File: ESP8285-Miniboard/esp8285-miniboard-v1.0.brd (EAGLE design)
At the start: 35.9 x 15.5 mm, 40 parts, among them Q1 FA-128

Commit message: Another Rev 1.0
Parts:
- moved C4 0.06 mm to (32.6, 22.0)
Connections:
- net N$IO1: now also PROG.2
- net N$IO2: no longer PROG.2
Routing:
- net N$IO2: track 23.4 -> 6.94 mm, vias 2 -> 0
- net N$IO1: track 20.2 -> 30.9 mm, vias 2 -> 3
- net N$IO3: track 24.6 -> 27.1 mm
- net N$3: track 1.55 -> 0.00 mm

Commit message: Hopefully final V1.0
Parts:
- added CH_PU: (no value), Ma-ESP8285:TESTPIN-HDR1X01
- moved 0 16.3 mm to (7.87, 14.2)
- moved 10 16.3 mm to (7.87, 1.46)
- moved 12 16.3 mm to (18.0, 14.2)
- moved 8 16.3 mm to (18.0, 1.46)
- moved R3 16.3 mm to (8.51, 8.45)
- moved 1 16.3 mm to (25.7, 1.46)
- moved 11 16.3 mm to (10.4, 1.46)
- moved 13 16.3 mm to (15.5, 14.2)
- moved 14 16.3 mm to (20.6, 14.2)
- moved 15 16.3 mm to (13.0, 14.2)
- moved 16 16.3 mm to (23.1, 14.2)
- moved 2 16.3 mm to (10.4, 14.2)
- moved 3 16.3 mm to (23.1, 1.46)
- moved 3V3 16.3 mm to (28.2, 14.2)
- moved 4 16.3 mm to (5.33, 14.2)
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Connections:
- net N$CHIP_PU: now also CH_PU.1
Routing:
- net GND: track 53.4 -> 74.1 mm, vias 9 -> 17
- net N$9: track 13.9 -> 0.00 mm
- net +3V3: track 65.4 -> 73.3 mm
- net N$4: track 7.00 -> 0.00 mm
- net N$7: track 5.84 -> 0.00 mm
- net N$5: track 4.23 -> 0.00 mm
- net N$IO1: track 30.9 -> 34.8 mm
- net N$IO15: track 14.6 -> 18.4 mm
- net N$IO3: track 27.1 -> 29.2 mm
- net N$6: track 1.44 -> 0.00 mm
- net N$CHIP_PU: track 11.4 -> 10.4 mm, vias 2 -> 1
- net N$IO2: track 6.94 -> 7.53 mm
- net N$IO0: track 22.9 -> 23.5 mm
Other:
- board text added: "Pwr"
- board text added: "Rx"
- board text added: "Tx"
- board text removed: "RX"
- board text removed: "TX"

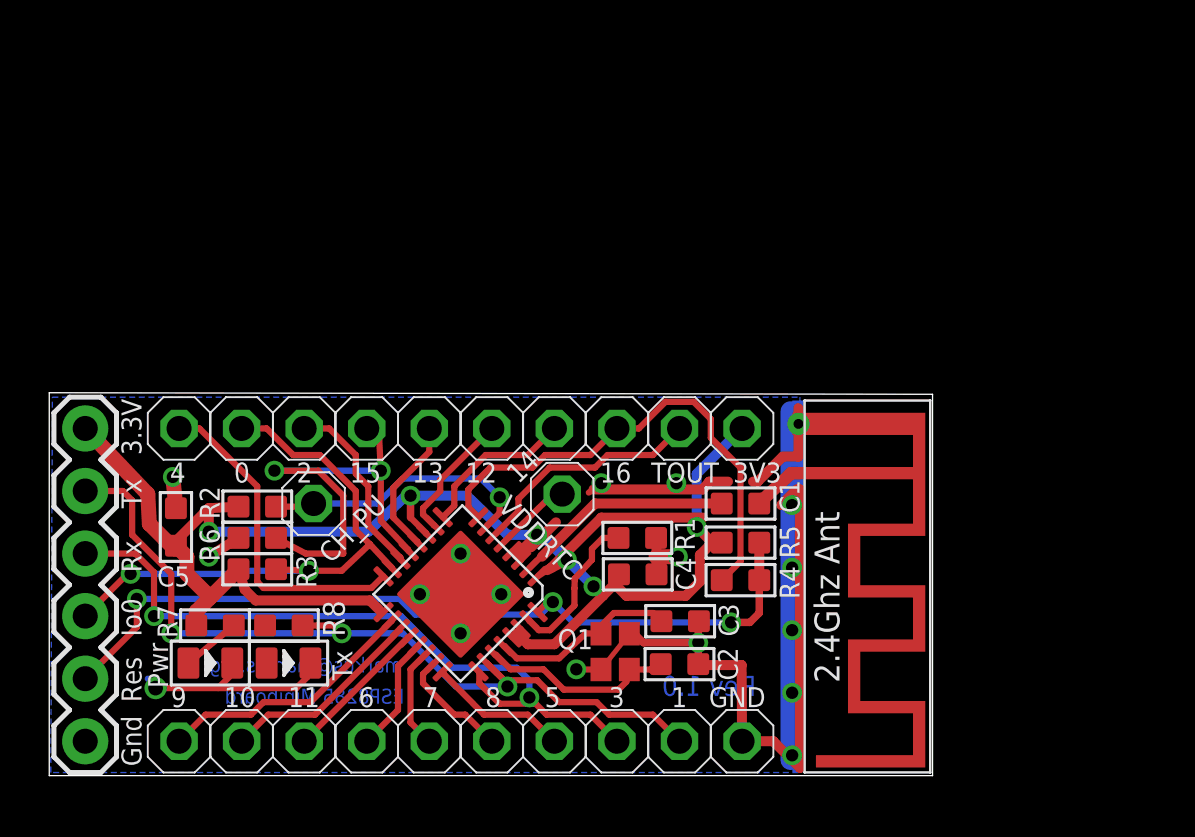
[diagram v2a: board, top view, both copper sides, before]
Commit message: Final v1.0 fixed silkscreen, added testpoint, reduced via size
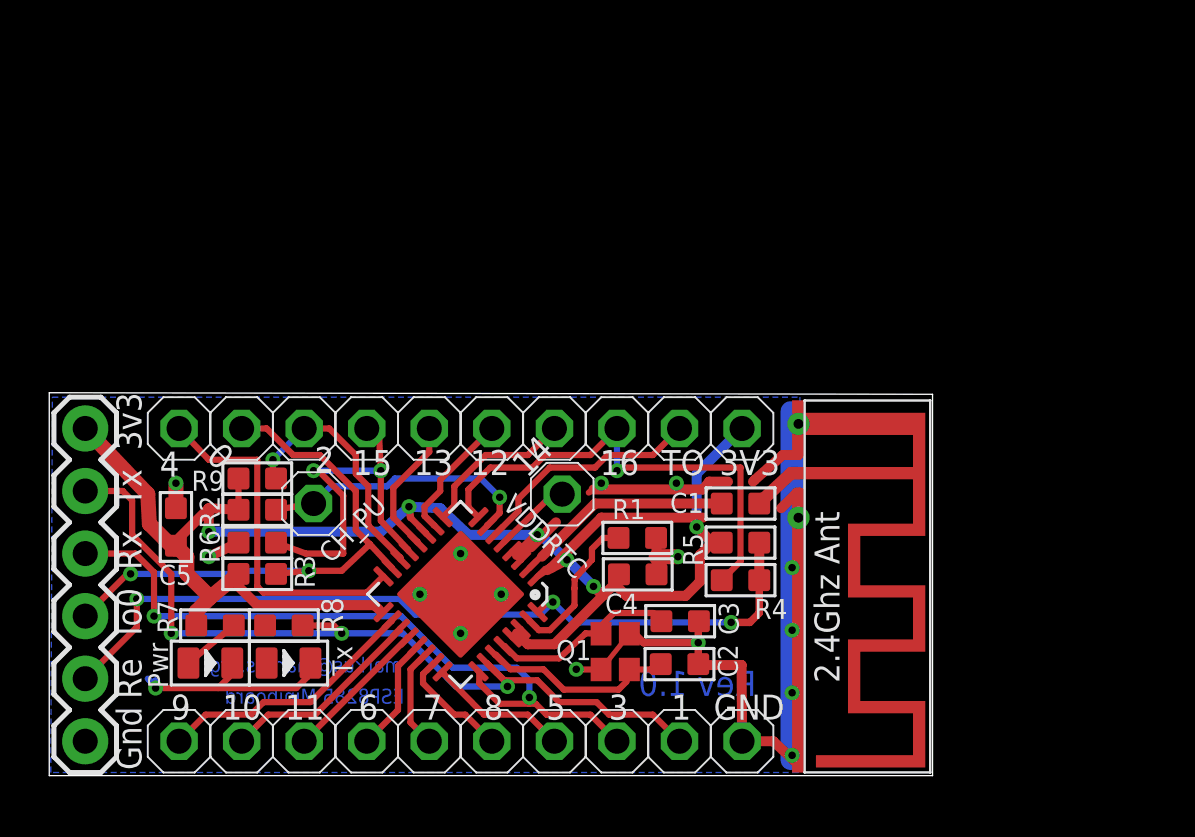
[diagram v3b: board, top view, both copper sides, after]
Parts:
- removed TOUT: (no value), Ma-ESP8285:TESTPIN-HDR1X01
- added R9: 10K, Seeed-OPL-Resistor:R0603
- added TO: (no value), Markus:TESTPIN-HDR1X01
- 0, 1, 10, 11, 12, 13, 14, 15, 16, 2, 3, 3V3, 4, 5, 6, 7, 8, 9, CH_PU, GND, VDDRTC: device Ma-ESP8285:TESTPIN-HDR1X01 -> Markus:TESTPIN-HDR1X01
- moved R6 0.19 mm to (8.51, 9.53)
- moved R3 0.19 mm to (8.51, 8.26)
- moved R2 0.13 mm to (8.51, 10.9)
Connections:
- net +3V3: now also R9.2
- net N$IO2: now also R9.1
- net N$TOUT: now also TO.1; no longer TOUT.1
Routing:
- net N$IO15: track 18.4 -> 15.2 mm
- net N$IO2: track 7.53 -> 10.2 mm, vias 0 -> 1
- net N$IO4: track 13.4 -> 14.4 mm
- net GND: track 74.1 -> 75.0 mm, vias 17 -> 16
- net N$CHIP_PU: track 10.4 -> 11.3 mm
- net N$IO16: track 20.3 -> 20.1 mm, vias 0 -> 1
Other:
- board text added: "3v3"
- board text added: "Re"
- board text removed: "3.3V"
- board text removed: "Res"
